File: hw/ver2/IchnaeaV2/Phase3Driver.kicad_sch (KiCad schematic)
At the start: 21 parts, among them Q2 MCAC80N10Y, Q3 MCAC80N10Y, Q4 MCAC80N10Y, Q5 MCAC80N10Y, U2 HIP2210

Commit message: Trying to further compress power loop area
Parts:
- renumbered C6 to C18, C7 to C19, C8 to C20, C9 to C21, C10 to C22, C11 to C23, C42 to C44, C48 to C50, C54 to C56, C60 to C62, D2 to D4, L1 to L3, Q2 to Q10, Q3 to Q11, Q4 to Q12, Q5 to Q13, R4 to R12, R5 to R13, R6 to R14, R7 to R15, U2 to U4

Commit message: Not quite happy with the power stage just yet.
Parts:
- C18: value 4.7uF -> 10uF-25V; LCSC C19666 -> C96446
- C23, C44, C50, C56, C62: value 10uF -> 10uF-100v
- D4: value Z3V3 -> Z5V1; LCSC C5353025 -> C2903912
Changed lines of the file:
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@@
 			)
 		)
-		(property "Value" "10uF"
+		(property "Value" "10uF-100v"
 			(at 242.57 102.8699 0)
 			(effects
@@
 			)
 		)
-		(property "Value" "4.7uF"
+		(property "Value" "10uF-25V"
 			(at 87.63 97.7899 0)
 			(effects
@@
 			)
 		)
-		(property "LCSC" "C19666"
+		(property "LCSC" "C96446"
 			(at 91.44 96.52 0)
 			(effects
@@
 			)
 		)
-		(property "Value" "10uF"
+		(property "Value" "10uF-100v"
 			(at 231.14 102.8699 0)
 			(effects
@@
 			)
 		)
-		(property "Value" "10uF"
+		(property "Value" "10uF-100v"
 			(at 219.71 102.8699 0)
 			(effects
@@
 			)
 		)
-		(property "Value" "Z3V3"
+		(property "Value" "Z5V1"
 			(at 114.3 97.7899 90)
 			(effects
@@
 			)
 		)
-		(property "LCSC" "C5353025"
+		(property "LCSC" "C2903912"
 			(at 116.84 96.52 90)
 			(effects
@@
 			)
 		)
-		(property "Value" "10uF"
+		(property "Value" "10uF-100v"
 			(at 254 102.8699 0)
 			(effects
@@
 			)
 		)
-		(property "Value" "10uF"
+		(property "Value" "10uF-100v"
 			(at 265.43 102.8699 0)
 			(effects

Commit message: Sync work to main PC
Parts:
- removed C19: 100nF, Capacitor_SMD:C_0603_1608Metric, symbol Device:C
- removed D4: Z5V1, Diode_SMD:D_SOD-123, symbol Device:D_Zener
- added C25, C31: 10uF-100v, Capacitor_SMD:C_1210_3225Metric_Pad1.33x2.70mm_HandSolder, symbol Device:C
- added R68: 0, Resistor_SMD:R_0603_1608Metric, symbol Device:R_US
- added R69: 10k, Resistor_SMD:R_0603_1608Metric, symbol Device:R_US
- added R70: 6.2k, Resistor_SMD:R_0603_1608Metric, symbol Device:R_US
- R12: value 2k -> 0; LCSC (none) -> C21189
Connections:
- net GND: now also C25.2, C31.2, R70.2
- net PWM: now also R68.2; no longer U4.8 (PWM)
- net PWMEN: now also R12.2; no longer U4.7 (EN)
- net SNSD-: now also L3.1; no longer L3.2
- net VCC: now also R69.1; no longer R12.2
- net VHIGH: now also C25.1, C31.1
- net at C20.2, Q10.3 (S), Q11.1 (D)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: now also L3.2; no longer L3.1
- net at R12.1: now also U4.7 (EN); no longer U4.5 (VREF)
- new net: R69.2, R70.1, U4.5 (VREF)
- new net: R68.1, U4.8 (PWM)
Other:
- moved on the sheet: C18, C20, C21, C22, C23, C44, C50, C56, C62, L3, Q10, Q11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

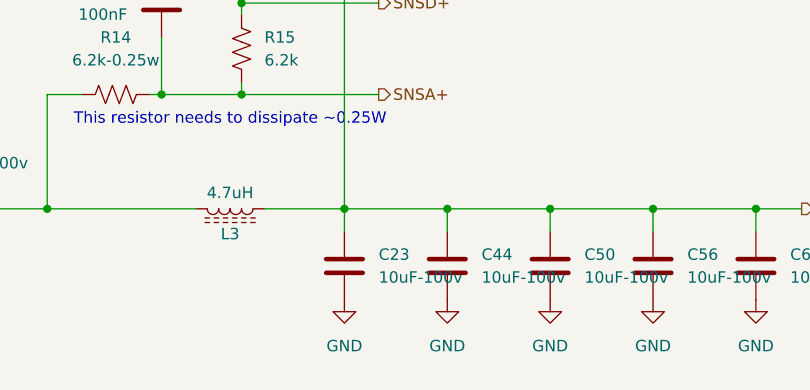
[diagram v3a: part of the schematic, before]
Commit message: More power stage layout
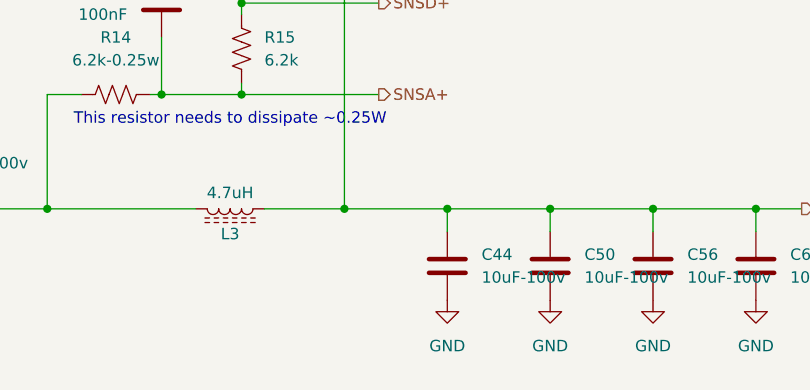
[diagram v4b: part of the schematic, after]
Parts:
- removed C23: 10uF-100v, Capacitor_SMD:C_1210_3225Metric_Pad1.33x2.70mm_HandSolder, symbol Device:C
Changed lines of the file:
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@@
-	(wire
-		(pts
-			(xy 186.69 95.25) (xy 186.69 97.79)
-		)
-		(stroke
-			(width 0)
-			(type default)
-		)
-	)
 	(wire
 		(pts
@@
 	(symbol
 		(lib_id "Device:C")
-		(at 186.69 101.6 0)
-		(unit 1)
-		(exclude_from_sim no)
-		(in_bom yes)
-		(on_board yes)
-		(dnp no)
-		(fields_autoplaced yes)
-		(property "Reference" "C23"
-			(at 190.5 100.3299 0)
-			(effects
-				(font
-					(size 1.27 1.27)
-				)
-				(justify left)
-			)
-		)
-		(property "Value" "10uF-100v"
-			(at 190.5 102.8699 0)
-			(effects
-				(font
-					(size 1.27 1.27)
-				)
-				(justify left)
-			)
-		)
-		(property "Footprint" "Capacitor_SMD:C_1210_3225Metric_Pad1.33x2.70mm_HandSolder"
-			(at 187.6552 105.41 0)
-			(effects
-				(font
-					(size 1.27 1.27)
-				)
-				(hide yes)
-			)
-		)
-		(property "Datasheet" "~"
-			(at 186.69 101.6 0)
-			(effects
-				(font
-					(size 1.27 1.27)
-				)
-				(hide yes)
-			)
-		)
-		(property "Description" "Unpolarized capacitor"
-			(at 186.69 101.6 0)
-			(effects
-				(font
-					(size 1.27 1.27)
-				)
-				(hide yes)
-			)
-		)
-		(property "Field-1" ""
-			(at 186.69 101.6 0)
-			(effects
-				(font
-					(size 1.27 1.27)
-				)
-				(hide yes)
-			)
-		)
-		(property "Digikey" "445-CGA6P1X7R1N106M250ACCT-ND"
-			(at 186.69 101.6 0)
-			(effects
-				(font
-					(size 1.27 1.27)
-				)
-				(hide yes)
-			)
-		)
-		(property "LCSC" "C576517"
-			(at 186.69 101.6 0)
-			(effects
-				(font
-					(size 1.27 1.27)
-				)
-				(hide yes)
-			)
-		)
-		(pin "1"
-		)
-		(pin "2"
-		)
-		(instances
-			(project "IchnaeaV2"
-				(path "/93408532-1ffa-463d-873c-16289d2b7987/31a930eb-86fc-490d-aa2b-31b72c4dd29d/48047d75-e488-4da1-b4d9-5027f5fb8795"
-					(reference "C23")
-					(unit 1)
-				)
-			)
-		)
-	)
-	(symbol
-		(lib_id "Device:C")
 		(at 93.98 91.44 0)
 		(unit 1)
@@
 					(unit 1)
 				)
-			)
-		)
-	)
-	(symbol
-		(lib_id "power:GND")
-		(at 186.69 105.41 0)
-		(unit 1)
-		(exclude_from_sim no)
-		(in_bom yes)
-		(on_board yes)
-		(dnp no)
-		(fields_autoplaced yes)
-		(property "Reference" "#PWR055"
-			(at 186.69 111.76 0)
-			(effects
-				(font
-					(size 1.27 1.27)
-				)
-				(hide yes)
-			)
-		)
-		(property "Value" "GND"
-			(at 186.69 110.49 0)
-			(effects
-				(font
-					(size 1.27 1.27)
-				)
-			)
-		)
-		(property "Footprint" ""
-			(at 186.69 105.41 0)
-			(effects
-				(font
-					(size 1.27 1.27)
-				)
-				(hide yes)
-			)
-		)
-		(property "Datasheet" ""
-			(at 186.69 105.41 0)
-			(effects
-				(font
-					(size 1.27 1.27)
-				)
-				(hide yes)
-			)
-		)
-		(property "Description" "Power symbol creates a global label with name \"GND\" , ground"
-			(at 186.69 105.41 0)
-			(effects
-				(font
-					(size 1.27 1.27)
-				)
-				(hide yes)
-			)
-		)
-		(pin "1"
-		)
-		(instances
-			(project "IchnaeaV2"
-				(path "/93408532-1ffa-463d-873c-16289d2b7987/31a930eb-86fc-490d-aa2b-31b72c4dd29d/48047d75-e488-4da1-b4d9-5027f5fb8795"
-					(reference "#PWR055")
-					(unit 1)
-				)

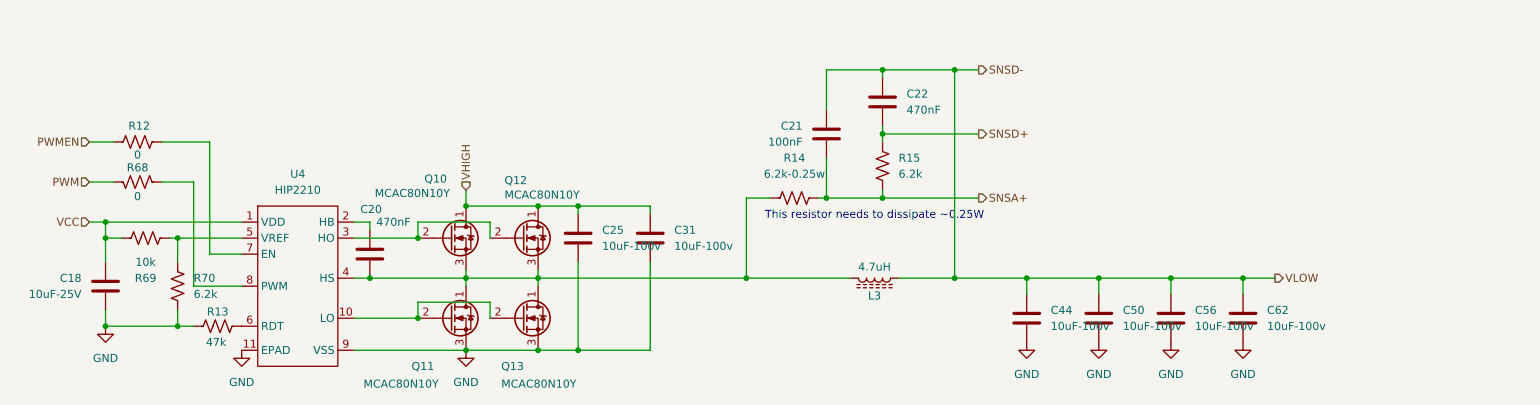
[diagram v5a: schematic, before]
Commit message: Partially work through the V1 notes. Start adding some of the control stage circuitry.
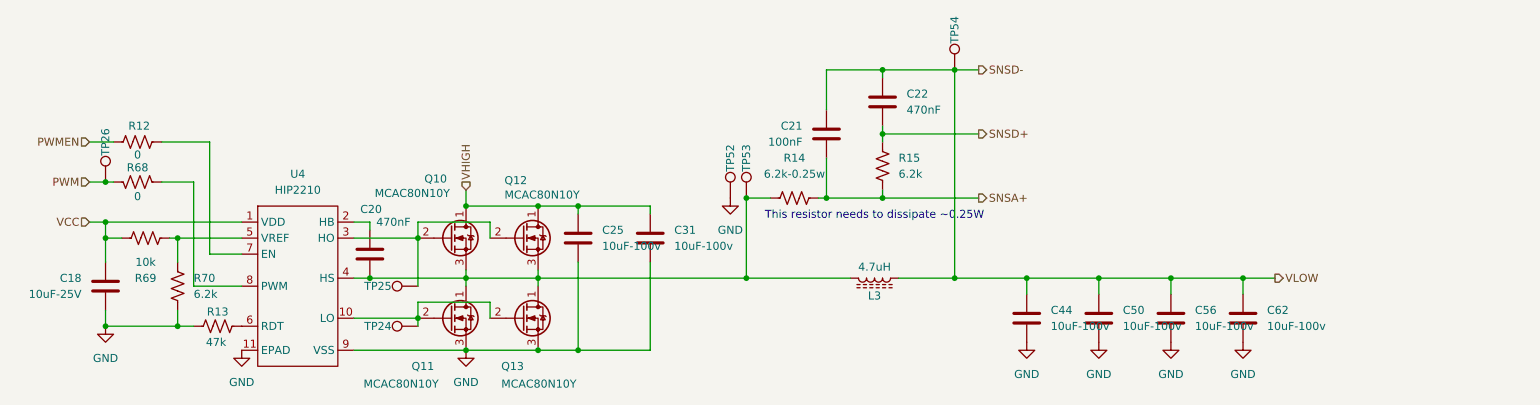
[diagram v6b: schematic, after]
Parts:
- added TP24, TP25, TP26, TP52, TP53, TP54: TestPoint, TestPoint:TestPoint_Pad_D1.0mm, symbol Connector:TestPoint
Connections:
- net GND: now also TP52.1
- net PWM: now also TP26.1
- net SNSD-: now also TP54.1
- net at C20.2, L3.2, Q10.3 (S)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: now also TP53.1
- net at Q11.2 (G), Q13.2 (G), U4.10 (LO): now also TP24.1
- net at Q10.2 (G), Q12.2 (G), U4.3 (HO): now also TP25.1
